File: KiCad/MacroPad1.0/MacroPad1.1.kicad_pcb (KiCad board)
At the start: 2 copper layers, 76.7 x 46 mm, 28 parts, among them SW1 SW_Push, U1 ATmega32U4-A, Y1 16MHz

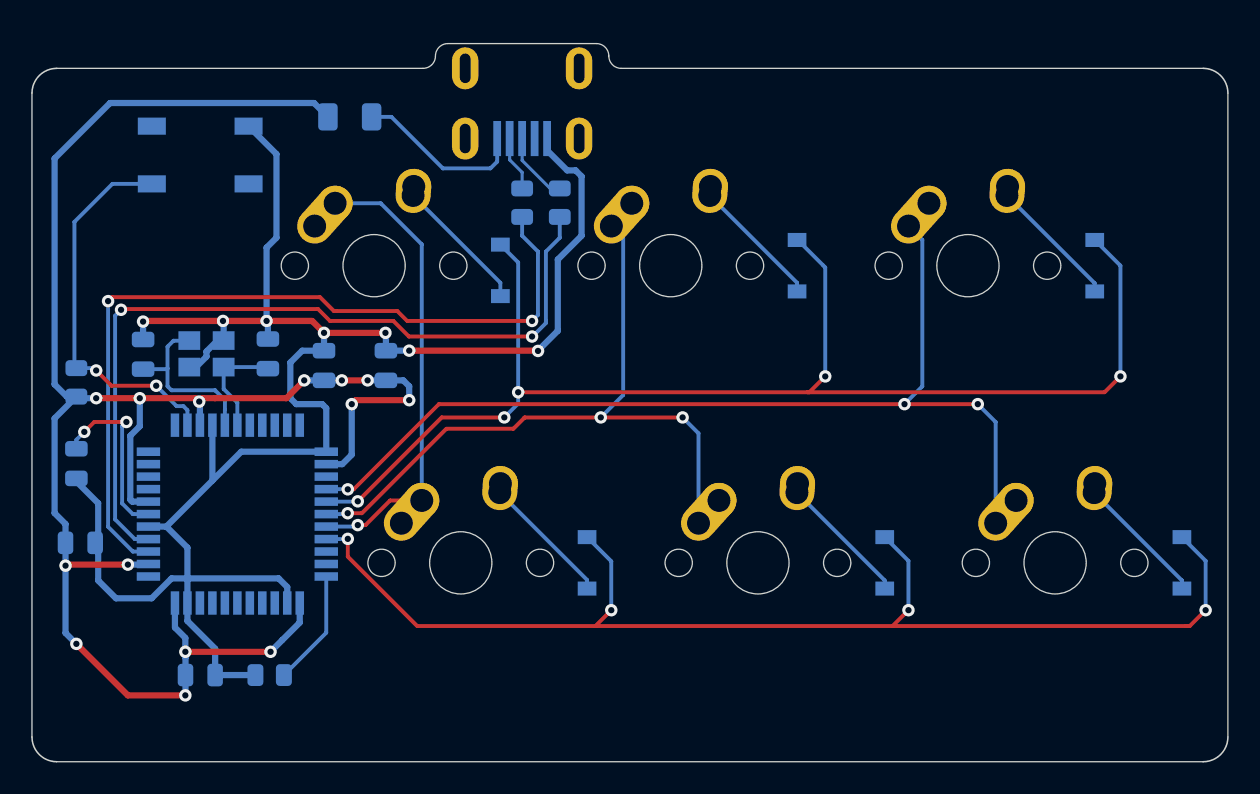
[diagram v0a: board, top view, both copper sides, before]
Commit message: Added ground mask
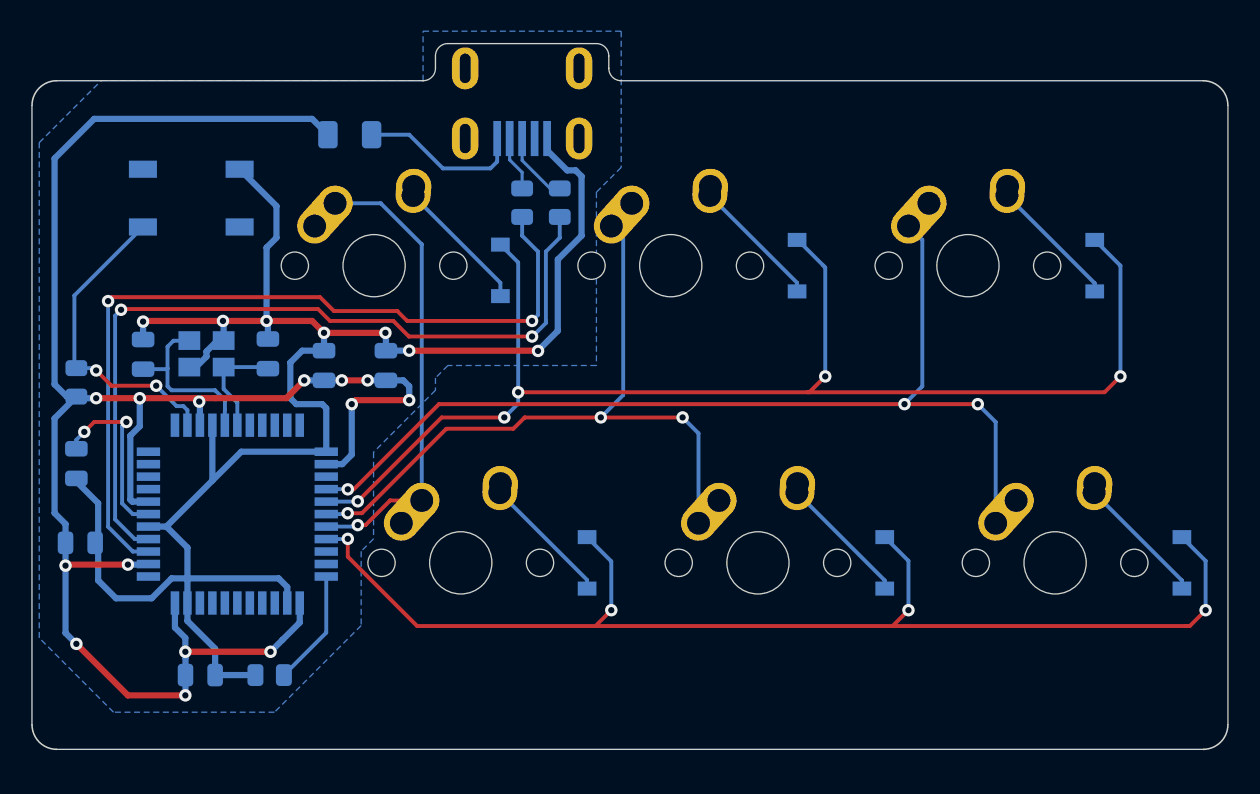
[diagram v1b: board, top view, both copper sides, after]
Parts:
- moved SW1 2.82 mm to (83.6, 79.8)
- moved F1 1.14 mm to (93.7, 75.7)
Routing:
- net Net-(R3-Pad1): track 24.6 -> 20.1 mm
- net GND: track 126.6 -> 124.0 mm
- added copper zone on B.Cu, net GND
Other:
- board size 76.7 x 46 mm -> 76.7 x 45.2 mm
- board text added: "MacroPad1.1"
- board text removed: "MacroPad1.0"
